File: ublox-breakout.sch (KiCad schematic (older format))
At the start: 45 parts, among them J1 Conn_02x06_Odd_Even, J2 Conn_Coaxial, J3 Conn_Coaxial, J4 USB_B_Micro, U1 74HCT2G125DP,125, U2 UBLOX_LEA-M8T-0, U3 USBLC6-4SC6, U4 XC6206P332MR, U5 XC6206P332MR

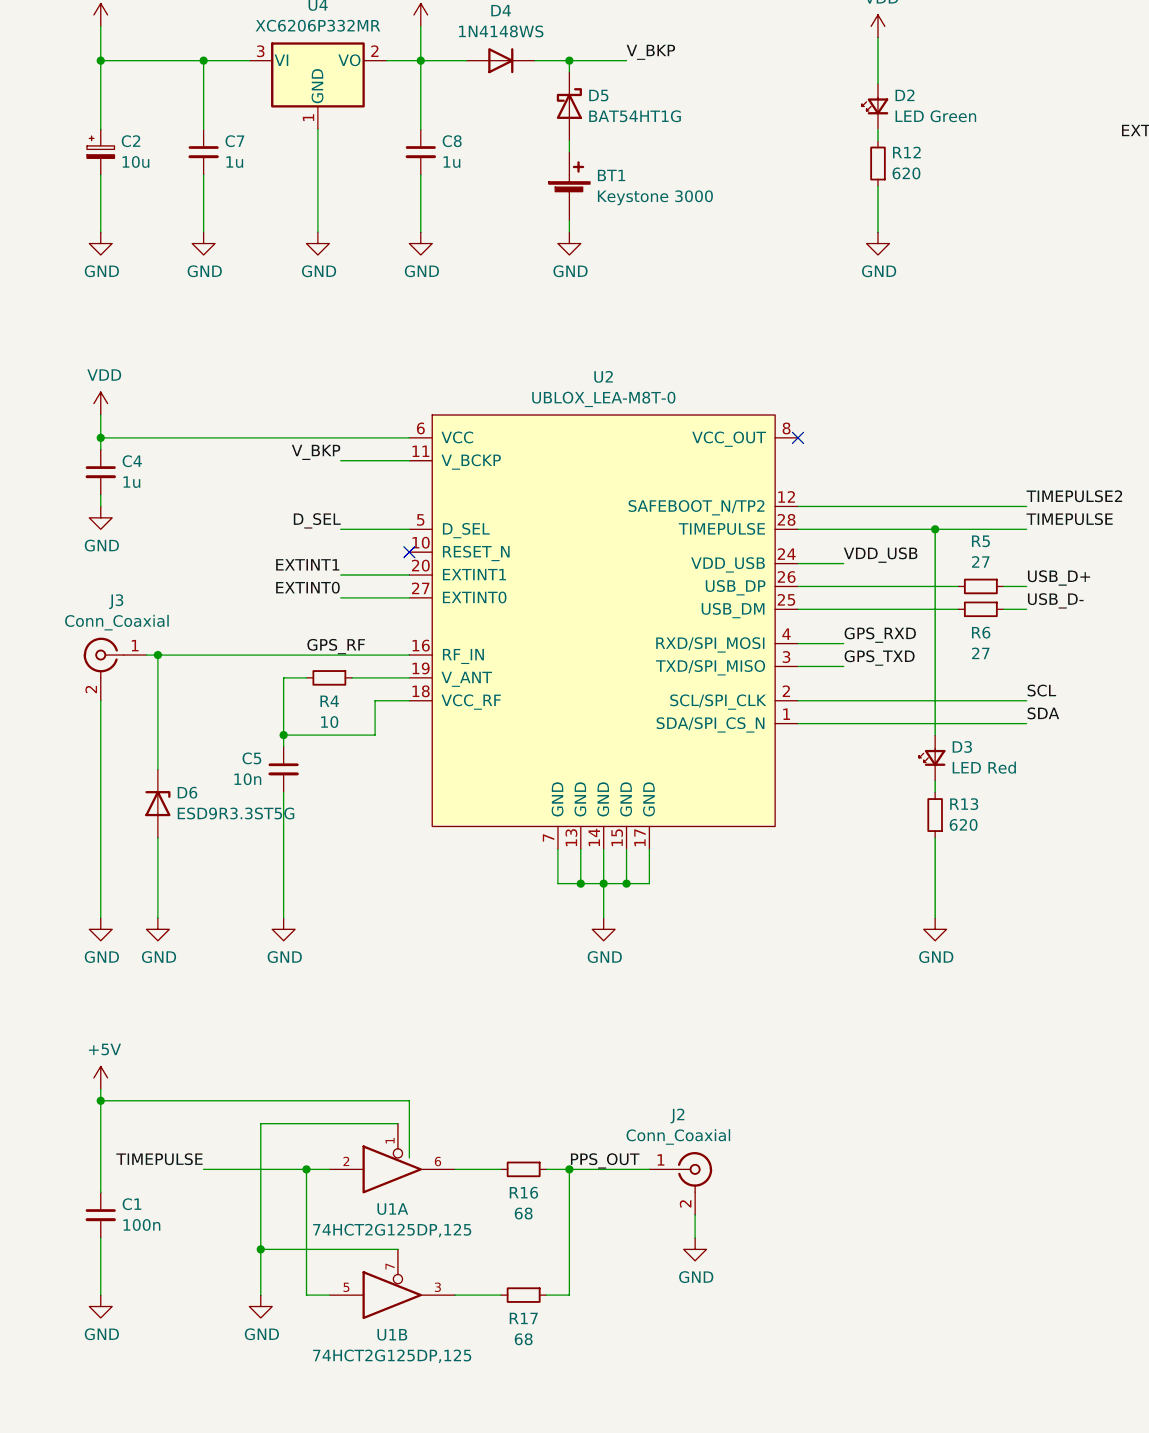
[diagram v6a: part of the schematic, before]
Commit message: Update PPS output buffer
Change output buffer to 2*NC7SZ125, add a small resistor network
to lift the input signal from 3.3V LVC to standard 5V CMOS
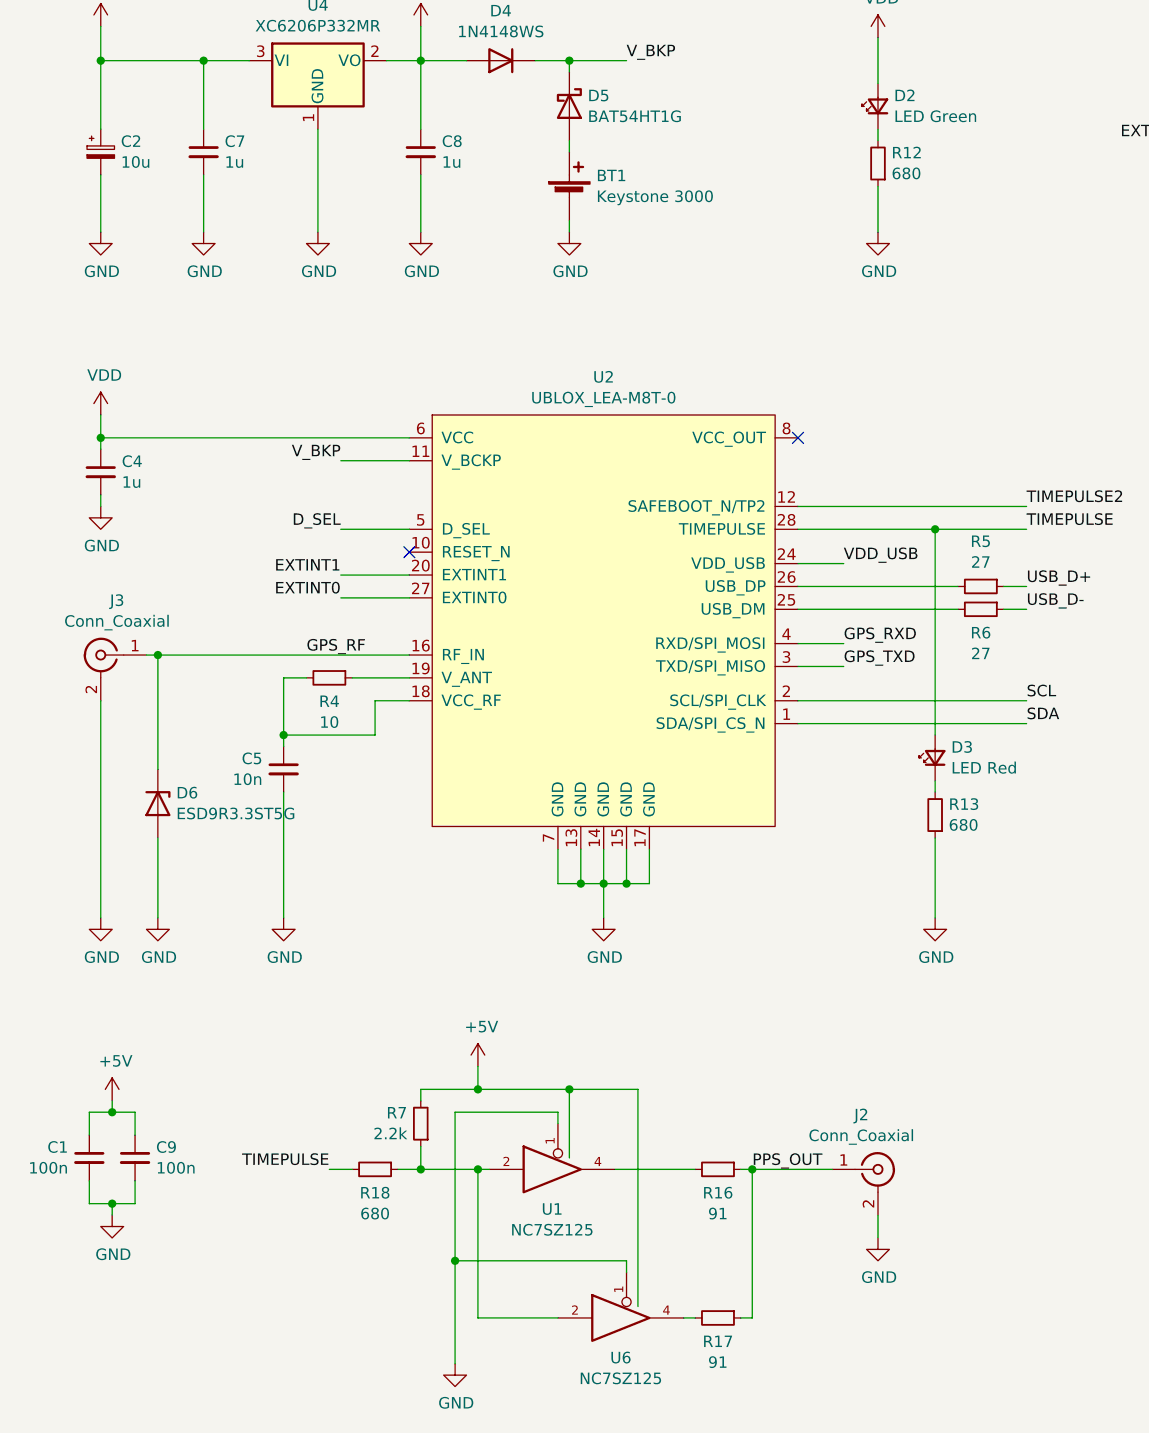
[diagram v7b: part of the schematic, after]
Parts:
- removed U1: 74HCT2G125DP,125, Package_SO:VSSOP-8_3.0x3.0mm_P0.65mm, symbol 74xGxx:74AUC2G125
- added C9: 100n, Capacitor_SMD:C_0603_1608Metric, symbol Device:C_Small
- added R18: 680, Resistor_SMD:R_0603_1608Metric, symbol Device:R_Small
- added R7: 2.2k, Resistor_SMD:R_0603_1608Metric, symbol Device:R_Small
- added U1, U6: NC7SZ125, Package_TO_SOT_SMD:SOT-353_SC-70-5, symbol 74xGxx:74LVC1G125
- C3, C4, C6, C7, C8: JLCPN C15849 -> C29936
- R12, R13: value 620 -> 680; JLCPN C23220 -> C23228
- R16, R17: value 68 -> 91; JLCPN C27592 -> C25199
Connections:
- net +5V: now also C9.1, R7.2, U1.5 (VCC), U6.5 (VCC)
- net GND: now also C9.2, U1.1, U1.3 (GND), U6.1, U6.3 (GND)
- net TIMEPULSE: now also R18.2
- net at R16.2: now also U1.4
- net at R17.2: now also U6.4
- new net: R18.1, R7.1, U1.2, U6.2
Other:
- moved on the sheet: C1, J2, R16, R17

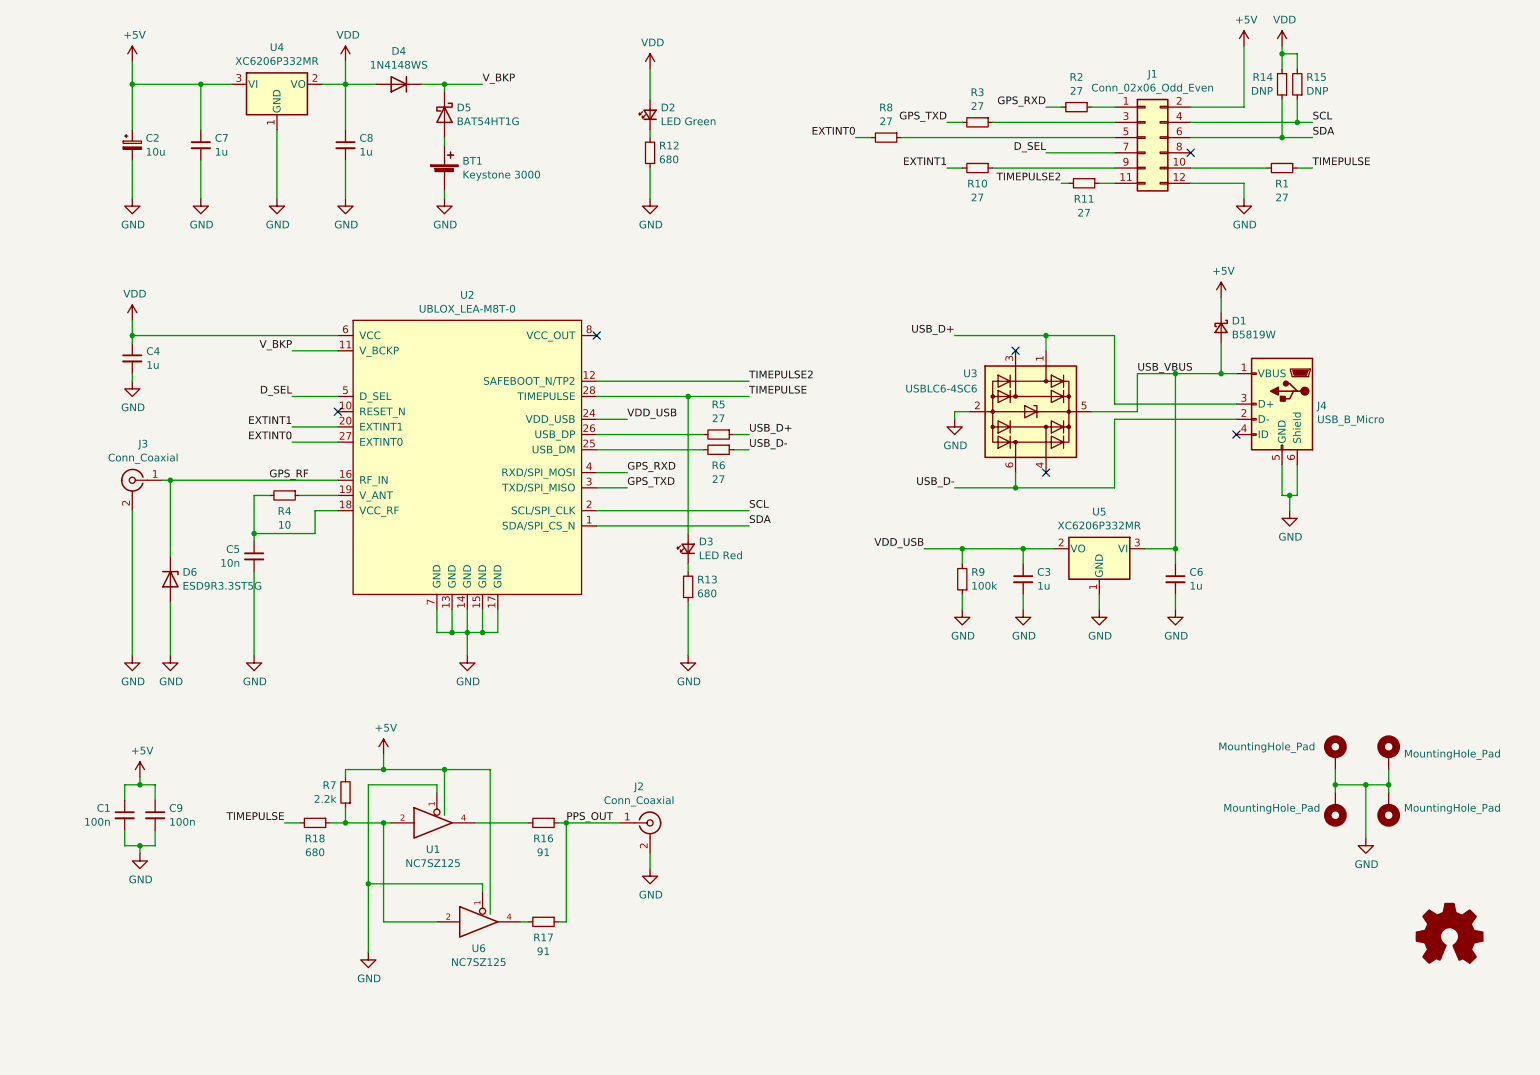
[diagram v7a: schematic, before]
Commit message: Overvoltage and R.P. protection, PPS buffer updates
Added an ESD diode at the input to protect the bulk
decoupling capacitor (tantalum). It's unidirectional and provides
at least some reverse polarity protection as well (will short out).

Faster rise time at input gate of PPS buffers by adding a small
10nF capacitor

Move USB ESD protection a bit to make soldering the USB receptacle
easier
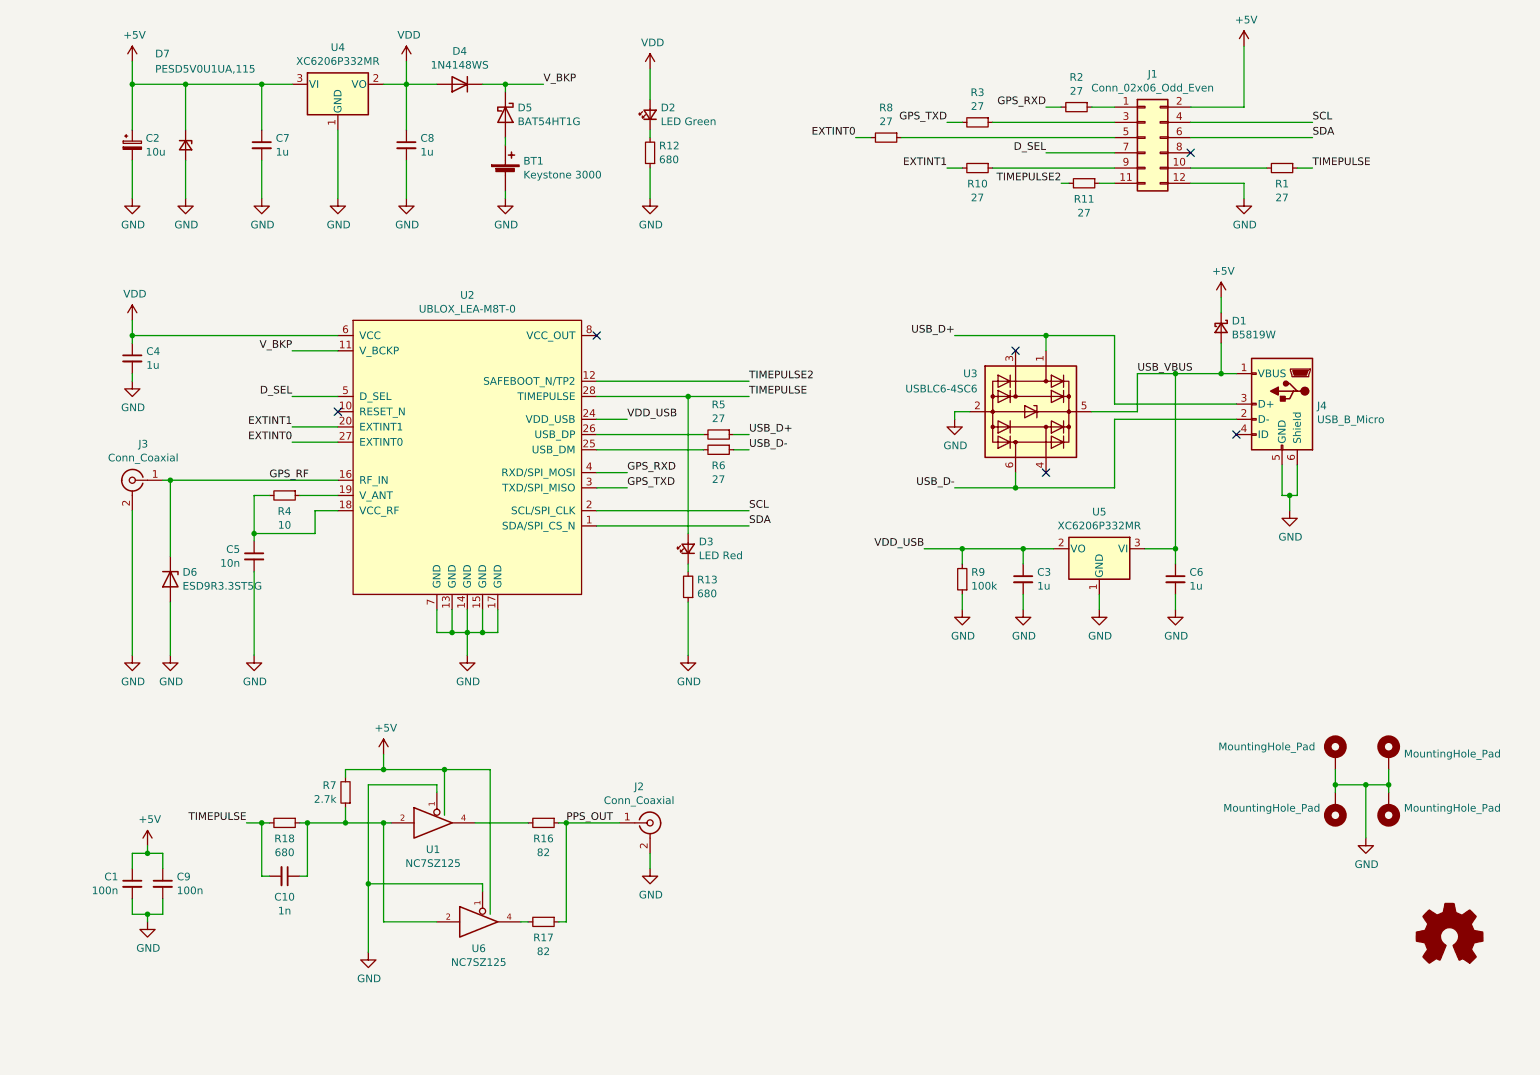
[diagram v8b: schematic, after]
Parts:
- removed R14, R15: DNP, Resistor_SMD:R_0603_1608Metric, symbol Device:R_Small
- added C10: 1n, Capacitor_SMD:C_0603_1608Metric, symbol Device:C_Small
- added D7: PESD5V0U1UA,115, Diode_SMD:D_SOD-323, symbol Device:D_Zener_Small
- R16, R17: value 91 -> 82; JLCPN C25199 -> C23255
- R7: value 2.2k -> 2.7k; JLCPN C4190 -> C13167
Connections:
- net +5V: now also D7.1 (K)
- net GND: now also D7.2 (A)
- net TIMEPULSE: now also C10.2
- net at R18.1, R7.1, U1.2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: now also C10.1
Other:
- moved on the sheet: BT1, C1, C7, C8, C9, D4, D5, R18, U4
